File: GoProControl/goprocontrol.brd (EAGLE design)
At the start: 35.2 x 74.9 mm, 17 parts, among them Q1 IRLML6344

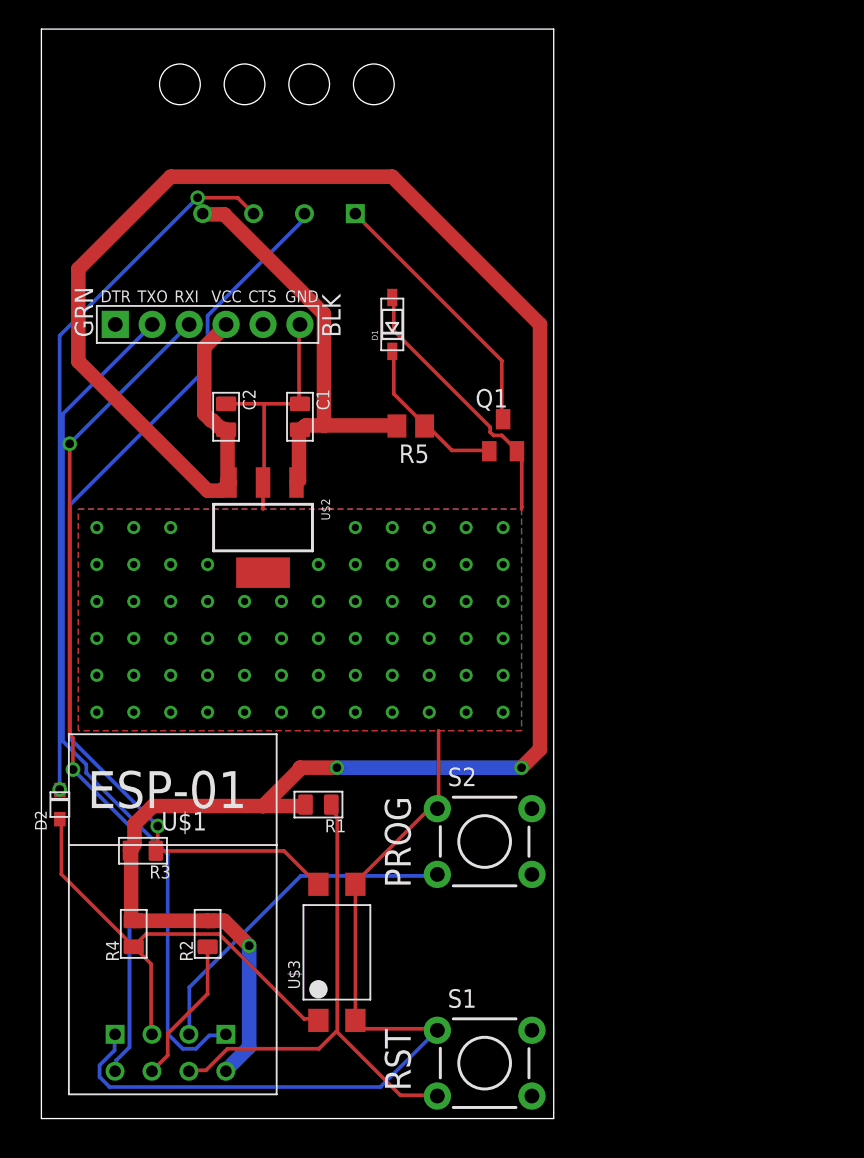
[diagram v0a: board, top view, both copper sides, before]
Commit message: update board to fit in sv650 ecu decoder box
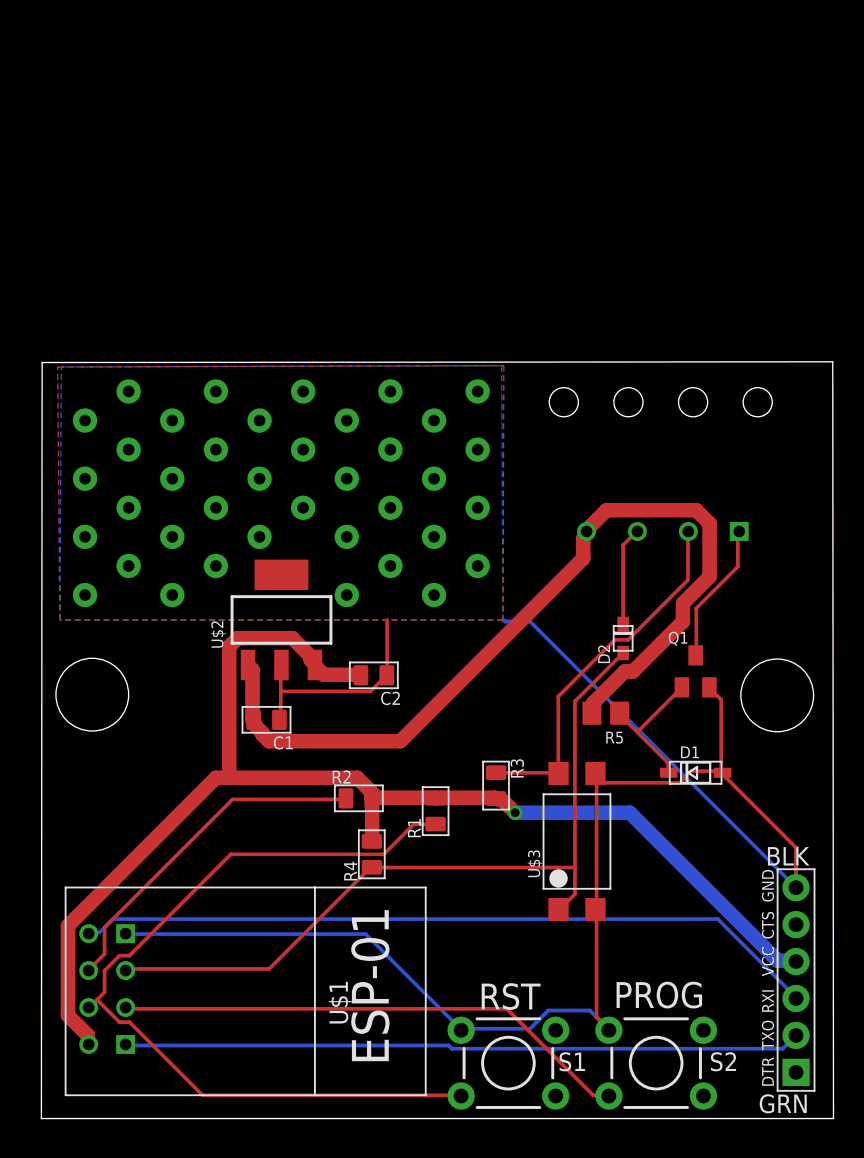
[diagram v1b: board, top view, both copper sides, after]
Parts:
- moved JP1 60.6 mm to (51.9, 9.53), turned to 90 degrees
- moved D2 40.4 mm to (40.0, 33.0)
- moved D1 37.2 mm to (45.0, 23.8), turned to 0 degrees
- moved U$4 34.3 mm to (48.0, 40.4)
- moved R3 24.7 mm to (31.3, 22.9), turned to 0 degrees
- moved R5 23.9 mm to (38.8, 27.9)
- moved C1 21.0 mm to (15.5, 27.4), turned to 270 degrees
- moved Q1 21.0 mm to (45.0, 30.8)
- moved C2 20.5 mm to (22.9, 30.5), turned to 270 degrees
- moved S2 19.3 mm to (42.3, 3.81)
- moved U$3 18.2 mm to (36.8, 19.1)
- moved R4 17.3 mm to (22.7, 18.2)
- moved R2 14.0 mm to (21.8, 22.0), turned to 90 degrees
- moved R1 8.07 mm to (27.1, 21.1), turned to 180 degrees
- moved U$2 6.48 mm to (16.5, 34.3), turned to 0 degrees
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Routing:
- net 3.3V: track 158.7 -> 91.0 mm, vias 3 -> 1
- net INPUT: track 49.0 -> 6.78 mm, vias 2 -> 0
- net OUTPUT: track 65.2 -> 25.2 mm, vias 1 -> 0
- net +12V: track 29.4 -> 60.8 mm
- net GND: track 93.9 -> 124.3 mm, vias 66 -> 38
- net N$3: track 35.8 -> 57.7 mm
- net GPIO2: track 33.0 -> 53.4 mm
- net N$1: track 10.1 -> 23.7 mm
- net TXD: track 59.1 -> 46.6 mm
- net GPIO0: track 23.6 -> 35.8 mm
- net GND_MAIN: track 18.4 -> 9.80 mm
- net RXD: track 56.9 -> 51.4 mm, vias 3 -> 0
- net N$17: track 11.3 -> 9.82 mm
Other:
- board size 35.2 x 74.9 mm -> 54.5 x 52 mm

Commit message: added ground planes top & bottom
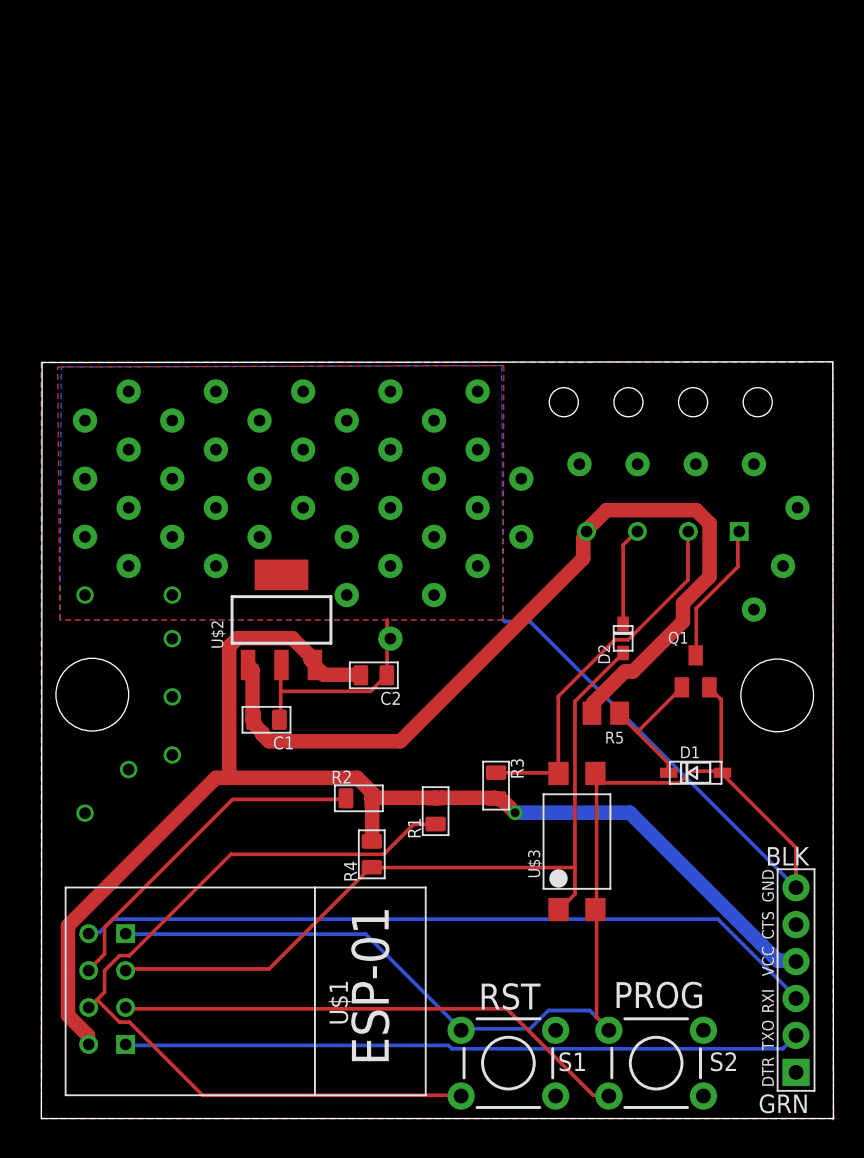
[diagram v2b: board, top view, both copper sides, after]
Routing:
- net GND: vias 38 -> 53
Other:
- board text added: "GoProControl v0.1 http://synfin.net/goprocontrol"
- board text added: "S/N:"
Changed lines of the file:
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@@
 <hole x="3.5" y="29.15" drill="5"/>
 <hole x="50.6" y="29.1" drill="5"/>
+<text x="48" y="16" size="1.016" layer="52" rot="MR0">GoProControl v0.1
+http://synfin.net/goprocontrol</text>
+<text x="48" y="11.5" size="1.778" layer="52" rot="MR0">S/N:</text>
+<rectangle x1="25" y1="10" x2="42" y2="15" layer="52"/>
 </plain>
 <attributes>
@@
 <vertex x="1.27" y="34.29"/>
 </polygon>
-<via x="3" y="36" extent="1-16" drill="0.8" diameter="1.6764" shape="square"/>
+<via x="3" y="36" extent="1-16" drill="0.8"/>
 <via x="3" y="40" extent="1-16" drill="0.8" diameter="1.6764" shape="square"/>
 <via x="3" y="44" extent="1-16" drill="0.8" diameter="1.6764" shape="square"/>
@@
 <via x="6" y="42" extent="1-16" drill="0.8" diameter="1.6764" shape="square"/>
 <via x="6" y="38" extent="1-16" drill="0.8" diameter="1.6764" shape="square"/>
-<via x="9" y="36" extent="1-16" drill="0.8" diameter="1.6764" shape="square"/>
+<via x="9" y="36" extent="1-16" drill="0.8"/>
 <via x="9" y="40" extent="1-16" drill="0.8" diameter="1.6764" shape="square"/>
 <via x="9" y="44" extent="1-16" drill="0.8" diameter="1.6764" shape="square"/>
@@
 <wire x1="28.9179" y1="6.1722" x2="28.8638" y2="6.0706" width="0.254" layer="16"/>
 <wire x1="38.9763" y1="6.1722" x2="39.0238" y2="6.0706" width="0.254" layer="16"/>
+<polygon width="0.254" layer="16">
+<vertex x="0" y="52"/>
+<vertex x="0" y="0"/>
+<vertex x="54.4" y="0"/>
+<vertex x="54.4" y="-0.1"/>
+<vertex x="54.45" y="-0.1"/>
+<vertex x="54.45" y="52"/>
+</polygon>
+<polygon width="0.254" layer="1">
+<vertex x="0" y="52"/>
+<vertex x="0" y="0"/>
+<vertex x="54.55" y="0"/>
+<vertex x="54.55" y="0.05"/>
+<vertex x="54.45" y="0.05"/>
+<vertex x="54.45" y="52"/>
+</polygon>
+<via x="9" y="33" extent="1-16" drill="0.8"/>
+<via x="9" y="29" extent="1-16" drill="0.8"/>
+<via x="9" y="25" extent="1-16" drill="0.8"/>
+<via x="6" y="24" extent="1-16" drill="0.8"/>
+<via x="3" y="21" extent="1-16" drill="0.8"/>
+<via x="33" y="44" extent="1-16" drill="0.8" diameter="1.6764" shape="square"/>
+<via x="33" y="40" extent="1-16" drill="0.8" diameter="1.6764" shape="square"/>
+<via x="37" y="45" extent="1-16" drill="0.8" diameter="1.6764" shape="square"/>
+<via x="41" y="45" extent="1-16" drill="0.8" diameter="1.6764" shape="square"/>
+<via x="45" y="45" extent="1-16" drill="0.8" diameter="1.6764" shape="square"/>
+<via x="49" y="45" extent="1-16" drill="0.8" diameter="1.6764" shape="square"/>
+<via x="52" y="42" extent="1-16" drill="0.8" diameter="1.6764" shape="square"/>
+<via x="51" y="38" extent="1-16" drill="0.8" diameter="1.6764" shape="square"/>
+<via x="49" y="35" extent="1-16" drill="0.8" diameter="1.6764" shape="square"/>
+<via x="24" y="33" extent="1-16" drill="0.8" diameter="1.6764" shape="square"/>
 </signal>
 <signal name="3.3V" class="2">
@@
 </board>
 </drawing>
+<compatibility>
+<note version="6.3" minversion="6.2.2" severity="warning">
+Since Version 6.2.2 text objects can contain more than one line,
+which will not be processed correctly with this version.
+</note>
+</compatibility>
 </eagle>

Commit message: v0.1 release
Fixed outline for term block and labled pins
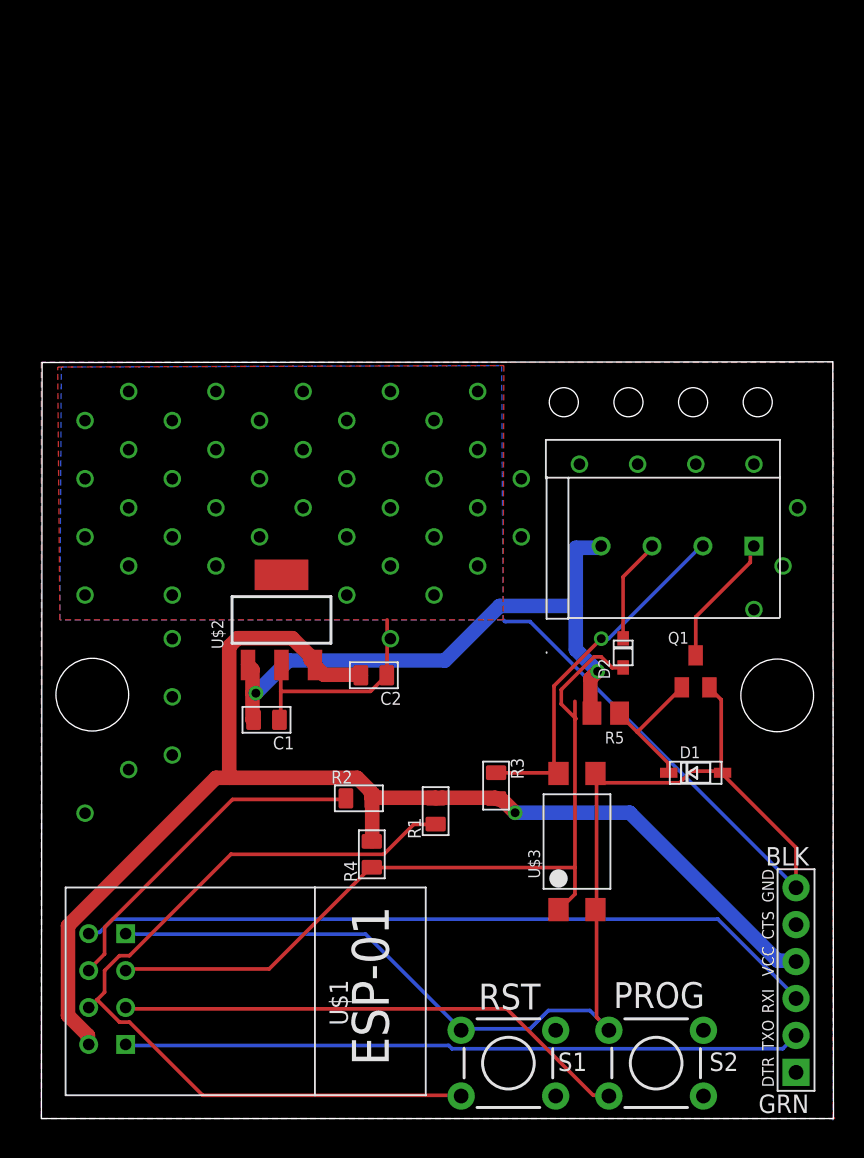
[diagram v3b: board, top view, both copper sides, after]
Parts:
- U$4: value PTSA-1.5/4-3.5F -> PTSA-1.5/4-3.5F4-3.5IP-2; device synfinatic:4-3.5IP -> synfinatic:4-3.5IP-2
- moved U$4 1.41 mm to (49.0, 39.4)
- moved D2 1.00 mm to (40.0, 32.0)
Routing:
- net +12V: track 60.8 -> 42.7 mm, vias 0 -> 2
- net GPIO2: track 53.4 -> 56.7 mm
- net GND_MAIN: track 9.80 -> 9.22 mm
- net OUTPUT: track 25.2 -> 24.8 mm, vias 0 -> 1
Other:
- board text added: "5-12V"
- board text added: "GND"
- board text added: "IN"
- board text added: "OUT"

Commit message: v0.2 small tweaks
- trim board to better fit case
- verify all DRC/ERC
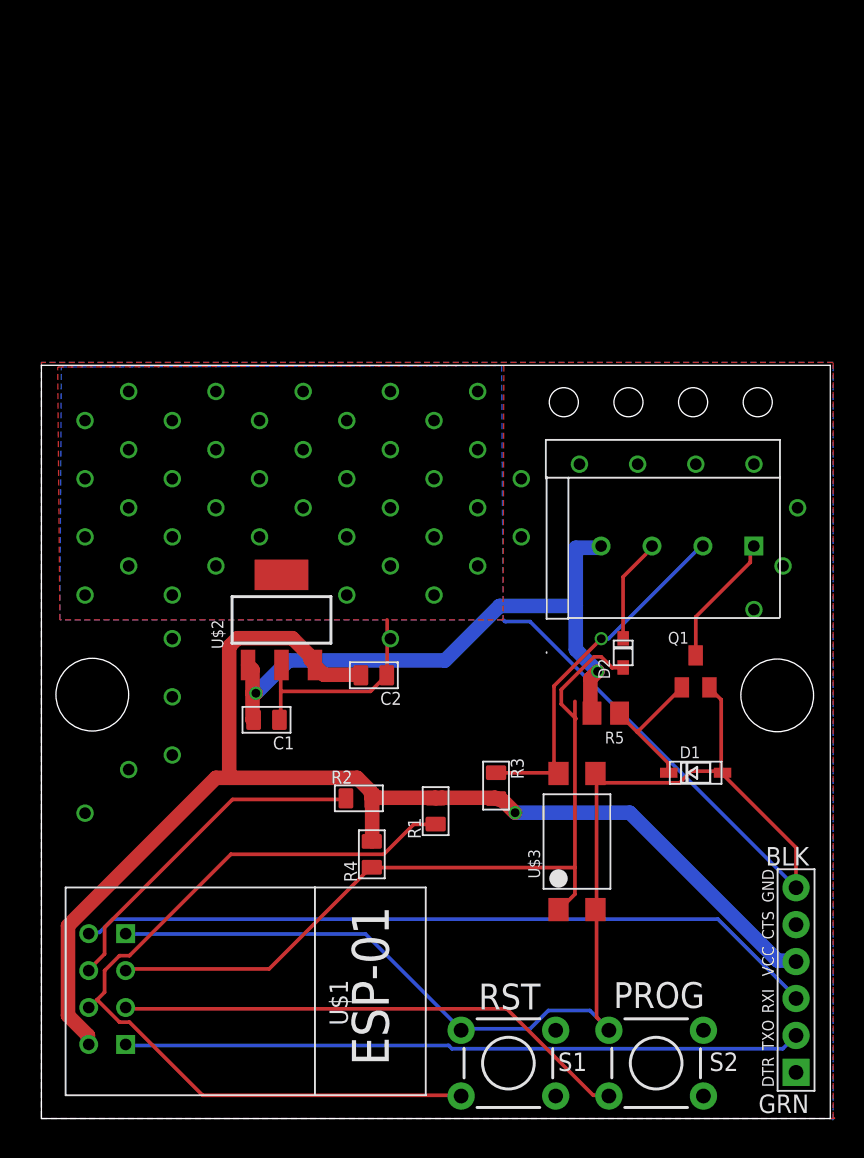
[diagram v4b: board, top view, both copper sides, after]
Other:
- board size 54.5 x 52 mm -> 54.2 x 51.8 mm
- board text added: "GoProControl v0.2 http://synfin.net/goprocontrol"
- board text removed: "GoProControl v0.1 http://synfin.net/goprocontrol"
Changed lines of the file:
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@@
 <board>
 <plain>
-<wire x1="0" y1="0" x2="54.47" y2="0" width="0" layer="20"/>
-<wire x1="54.47" y1="0" x2="54.42" y2="52.04" width="0" layer="20"/>
-<wire x1="54.42" y1="52.04" x2="0.05" y2="51.99" width="0" layer="20"/>
-<wire x1="0.05" y1="51.99" x2="0" y2="0" width="0" layer="20"/>
+<wire x1="0" y1="0" x2="54.25" y2="0" width="0" layer="20"/>
+<wire x1="54.25" y1="0" x2="54.25" y2="51.8" width="0" layer="20"/>
+<wire x1="54.25" y1="51.8" x2="0" y2="51.8" width="0" layer="20"/>
+<wire x1="0" y1="51.8" x2="0" y2="0" width="0" layer="20"/>
 <text x="34.32" y="9.28" size="1.778" layer="25" rot="R180">RST</text>
 <text x="45.615" y="9.38" size="1.778" layer="25" rot="R180">PROG</text>
@@
 <hole x="3.5" y="29.15" drill="5"/>
 <hole x="50.6" y="29.1" drill="5"/>
-<text x="48" y="16" size="1.016" layer="26" rot="MR0">GoProControl v0.1
+<text x="48" y="16" size="1.016" layer="26" rot="MR0">GoProControl v0.2
 http://synfin.net/goprocontrol</text>
 <text x="48" y="11.5" size="1.778" layer="26" rot="MR0">S/N:</text>
@@
 </class>
 </classes>
-<designrules name="default">
+<designrules name="SeeedStudio_2layer_DRU_no_angle_20140221 *">
 <description language="de">&lt;b&gt;EAGLE Design Rules&lt;/b&gt;
 &lt;p&gt;
@@
 Einstellungen hier und speichern die Design Rules unter
 einem neuen Namen ab.</description>
-<description language="en">&lt;b&gt;EAGLE Design Rules&lt;/b&gt;
-&lt;p&gt;
-The default Design Rules have been set to cover
-a wide range of applications. Your particular design
-may have different requirements, so please make the
-necessary adjustments and save your customized
-design rules under a new name.</description>
+<description language="en">&lt;b&gt;SeeedStudio Design Rules&lt;/b&gt;
+</description>
+<description language="zh">&lt;b&gt;Seeed Studio EAGLE Design Rules&lt;/b&gt;
+</description>
 <param name="layerSetup" value="(1*16)"/>
-<param name="mtCopper" value="0.035mm 0.035mm 0.035mm 0.035mm 0.035mm 0.035mm 0.035mm 0.035mm 0.035mm 0.035mm 0.035mm 0.035mm 0.035mm 0.035mm 0.035mm 0.035mm"/>
-<param name="mtIsolate" value="1.5mm 0.15mm 0.2mm 0.15mm 0.2mm 0.15mm 0.2mm 0.15mm 0.2mm 0.15mm 0.2mm 0.15mm 0.2mm 0.15mm 0.2mm"/>
-<param name="mdWireWire" value="8mil"/>
-<param name="mdWirePad" value="8mil"/>
-<param name="mdWireVia" value="8mil"/>
-<param name="mdPadPad" value="8mil"/>
-<param name="mdPadVia" value="8mil"/>
-<param name="mdViaVia" value="8mil"/>
-<param name="mdSmdPad" value="8mil"/>
-<param name="mdSmdVia" value="8mil"/>
-<param name="mdSmdSmd" value="8mil"/>
+<param name="mtCopper" value="0.035mm 0.0175mm 0.035mm 0.035mm 0.035mm 0.035mm 0.035mm 0.035mm 0.035mm 0.035mm 0.035mm 0.035mm 0.035mm 0.035mm 0.0175mm 0.035mm"/>
+<param name="mtIsolate" value="1.5mm 1.1mm 0.2mm 0.15mm 0.2mm 0.15mm 0.2mm 0.15mm 0.2mm 0.15mm 0.2mm 0.15mm 0.2mm 0.15mm 0.2mm"/>
+<param name="mdWireWire" value="6mil"/>
+<param name="mdWirePad" value="6mil"/>
+<param name="mdWireVia" value="6mil"/>
+<param name="mdPadPad" value="6mil"/>
+<param name="mdPadVia" value="6mil"/>
+<param name="mdViaVia" value="6mil"/>
+<param name="mdSmdPad" value="0mil"/>
+<param name="mdSmdVia" value="0mil"/>
+<param name="mdSmdSmd" value="0mil"/>
 <param name="mdViaViaSameLayer" value="8mil"/>
 <param name="mnLayersViaInSmd" value="2"/>
-<param name="mdCopperDimension" value="40mil"/>
-<param name="mdDrill" value="8mil"/>
+<param name="mdCopperDimension" value="10mil"/>
+<param name="mdDrill" value="10mil"/>
 <param name="mdSmdStop" value="0mil"/>
-<param name="msWidth" value="10mil"/>
-<param name="msDrill" value="24mil"/>
-<param name="msMicroVia" value="9.99mm"/>
+<param name="msWidth" value="6mil"/>
+<param name="msDrill" value="12mil"/>
+<param name="msMicroVia" value="12mil"/>
 <param name="msBlindViaRatio" value="0.5"/>
 <param name="rvPadTop" value="0.25"/>
@@
 <param name="rlMinPadBottom" value="10mil"/>
 <param name="rlMaxPadBottom" value="20mil"/>
-<param name="rlMinViaOuter" value="8mil"/>
+<param name="rlMinViaOuter" value="6mil"/>
 <param name="rlMaxViaOuter" value="20mil"/>
-<param name="rlMinViaInner" value="8mil"/>
+<param name="rlMinViaInner" value="6mil"/>
 <param name="rlMaxViaInner" value="20mil"/>
 <param name="rlMinMicroViaOuter" value="4mil"/>
@@
 <param name="psTop" value="-1"/>
 <param name="psBottom" value="-1"/>
-<param name="psFirst" value="-1"/>
+<param name="psFirst" value="0"/>
 <param name="psElongationLong" value="100"/>
 <param name="psElongationOffset" value="100"/>
 <param name="mvStopFrame" value="1"/>
 <param name="mvCreamFrame" value="0"/>
-<param name="mlMinStopFrame" value="4mil"/>
-<param name="mlMaxStopFrame" value="4mil"/>
+<param name="mlMinStopFrame" value="2mil"/>
+<param name="mlMaxStopFrame" value="2mil"/>
 <param name="mlMinCreamFrame" value="0mil"/>
 <param name="mlMaxCreamFrame" value="0mil"/>
-<param name="mlViaStopLimit" value="0mil"/>
+<param name="mlViaStopLimit" value="100mil"/>
 <param name="srRoundness" value="0"/>
 <param name="srMinRoundness" value="0mil"/>
@@
 <param name="checkAngle" value="0"/>
 <param name="checkFont" value="1"/>
-<param name="checkRestrict" value="1"/>
+<param name="checkRestrict" value="0"/>
 <param name="useDiameter" value="13"/>
 <param name="maxErrors" value="50"/>
